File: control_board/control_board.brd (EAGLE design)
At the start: 63 x 73.3 mm, 65 parts, among them IC1 ATMEGA1284P-MU, J1 USB Female Type C Connector, J5 20021311-00010T4LF, J6 20021311-00010T4LF, J7 20021311-00010T4LF, Q2 BSS84-7-F, Q3 BSS138PW,115, SW1 SPST_TACT-KMR2, U1 915MHz, U3 MCP73833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

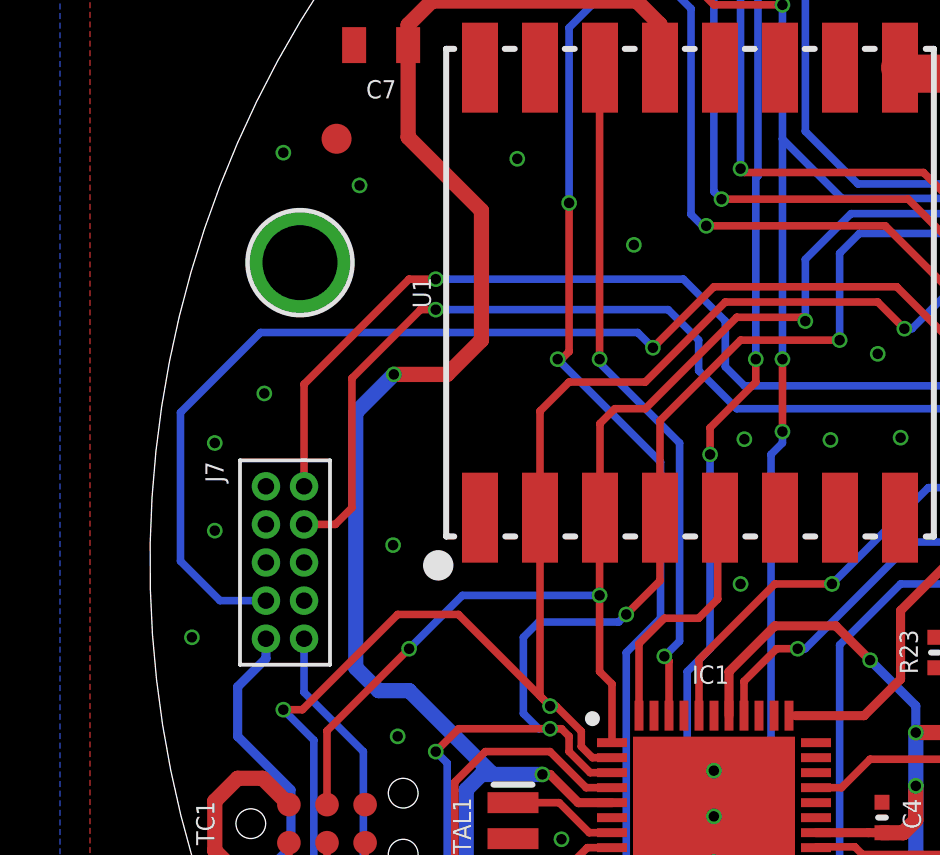
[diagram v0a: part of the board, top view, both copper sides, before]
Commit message: Added pullup on SS pin of radio
- Without pullup, bootloader can't be loaded
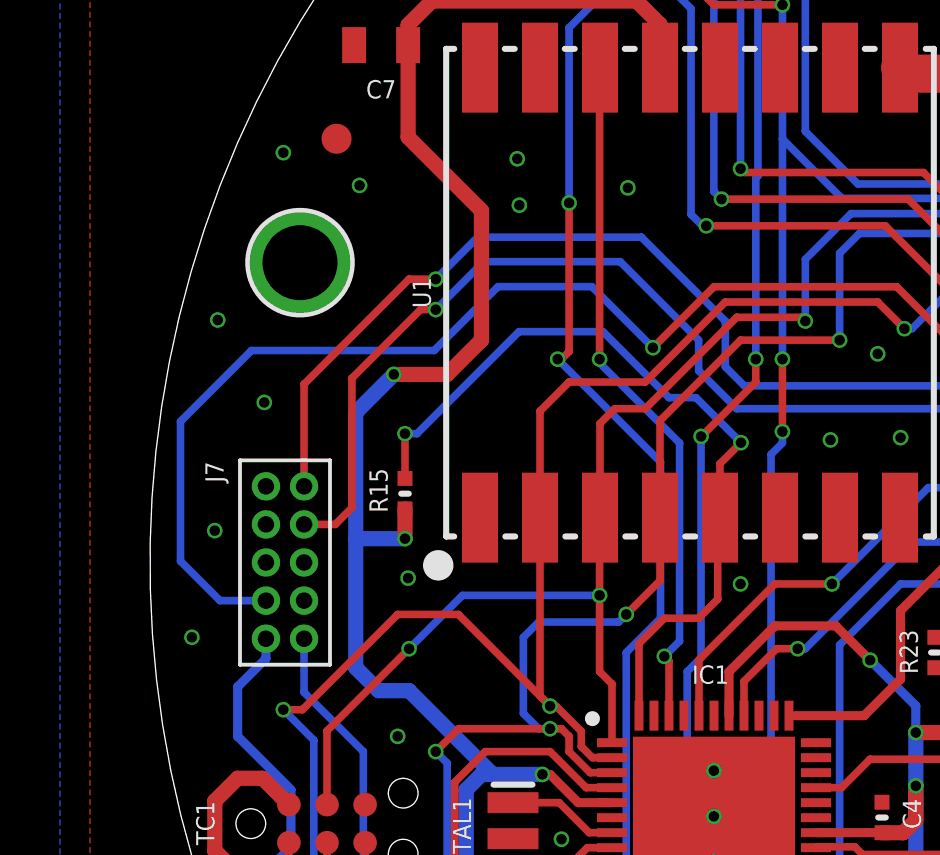
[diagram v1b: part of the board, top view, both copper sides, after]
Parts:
- added R15: 10K, Adafruit Feather 32u4 Bluefruit LE:MICROBUILDER__0402MP
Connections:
- net SS: now also R15.2
- net VCC: now also R15.1
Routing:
- net SS: track 8.39 -> 26.8 mm, vias 0 -> 2
- net VCC: track 175.3 -> 177.9 mm, vias 9 -> 10
- net MOTOR_CONTROL: track 53.8 -> 55.2 mm
- net CURRENT_SENSE_POWER: track 56.5 -> 57.7 mm
- net TEMP: track 56.2 -> 57.3 mm
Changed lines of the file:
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@@
 </layers>
 <board>
-<fusionsync huburn="a.YnVzaW5lc3M6aGF3azI1NA" projecturn="a.YnVzaW5lc3M6aGF3azI1NCMyMDIwMDkxNDMzMjY0NDc4MQ" f3durn="urn:adsk.wipprod:dm.lineage:UtJg9LLlSdqN8RmJzLy1Ng" pcbguid="012a3abc-d9c1-4d21-a72f-0cb22081b20e" lastpulledtime="" lastsyncedchangeguid="" latestrevisionid="7e68664b-9ece-4de8-8436-a87560e4c601" lastsyncedrevisionid="7e68664b-9ece-4de8-8436-a87560e4c601" lastboardhashguid="2f9d8b28-5ca6-9da8-7f9d-c0648b5d30e4" lastpushedtime="2020-11-20T05:35:07Z" linktopcb3d="true"/>
+<fusionsync huburn="a.YnVzaW5lc3M6aGF3azI1NA" projecturn="a.YnVzaW5lc3M6aGF3azI1NCMyMDIwMDkxNDMzMjY0NDc4MQ" f3durn="urn:adsk.wipprod:dm.lineage:UtJg9LLlSdqN8RmJzLy1Ng" pcbguid="" lastpulledtime="" lastsyncedchangeguid="" latestrevisionid="7e68664b-9ece-4de8-8436-a87560e4c601" lastsyncedrevisionid="7e68664b-9ece-4de8-8436-a87560e4c601" lastboardhashguid="2f9d8b28-5ca6-9da8-7f9d-c0648b5d30e4" lastpushedtime="2020-11-20T05:35:07Z" linktopcb3d="true"/>
 <plain>
 <wire x1="35" y1="75" x2="35" y2="-7" width="0.15" layer="49"/>
@@
 <attribute name="PROD_ID" value="CAP-08469" x="7.704" y="52.252" size="1.778" layer="27" display="off"/>
 </element>
+<element name="R15" library="Adafruit Feather 32u4 Bluefruit LE" package="MICROBUILDER__0402MP" override_package3d_urn="urn:adsk.eagle:package:24877243/2" override_package_urn="urn:adsk.eagle:footprint:24877244/1" value="10K" x="8.5" y="37.3" smashed="yes" rot="R90">
+<attribute name="MPN" value="RC0402FR-7W10KL" x="8.5" y="37.3" size="1.778" layer="27" rot="R90" display="off"/>
+<attribute name="NAME" x="7.9237" y="36.665" size="0.6096" layer="25" font="vector" rot="R90"/>
+</element>
 </elements>
 <signals>
@@
 <wire x1="13.081" y1="27.94" x2="11.43" y2="27.94" width="0.508" layer="16"/>
 <wire x1="7.62" y1="30.734" x2="6.858" y2="31.496" width="0.508" layer="16"/>
-<wire x1="6.858" y1="31.496" x2="6.858" y2="40.005" width="0.508" layer="16"/>
+<wire x1="6.858" y1="31.496" x2="6.858" y2="35.8" width="0.508" layer="16"/>
+<wire x1="6.858" y1="35.8" x2="6.858" y2="40.005" width="0.508" layer="16"/>
 <wire x1="6.858" y1="40.005" x2="8.128" y2="41.275" width="0.508" layer="16"/>
 <via x="8.128" y="41.275" extent="1-16" drill="0.35"/>
@@
 <wire x1="8.604" y1="52.252" x2="8.604" y2="52.927" width="0.508" layer="1"/>
 <wire x1="8.604" y1="52.927" x2="9.398" y2="53.721" width="0.508" layer="1"/>
+<contactref element="R15" pad="1"/>
+<wire x1="8.5" y1="36.792" x2="8.5" y2="35.8" width="0.508" layer="1"/>
+<via x="8.5" y="35.8" extent="1-16" drill="0.35"/>
+<wire x1="8.5" y1="35.8" x2="6.858" y2="35.8" width="0.508" layer="16"/>
 </signal>
 <signal name="GND" class="1">
@@
 <via x="26.67" y="30.353" extent="1-16" drill="0.35"/>
 <via x="34.29" y="36.703" extent="1-16" drill="0.35"/>
-<via x="16.129" y="45.593" extent="1-16" drill="0.35"/>
+<via x="15.929" y="47.493" extent="1-16" drill="0.35"/>
 <via x="38.0492" y="13.8684" extent="1-16" drill="0.35"/>
 <via x="38.862" y="13.4366" extent="1-16" drill="0.35"/>
@@
 <via x="6.985" y="47.5742" extent="1-16" drill="0.35"/>
 <via x="46.5074" y="51.0286" extent="1-16" drill="0.35"/>
-<via x="8.1026" y="35.5854" extent="1-16" drill="0.35"/>
+<via x="8.6026" y="34.4854" extent="1-16" drill="0.35"/>
 <via x="13.2842" y="18.5674" extent="1-16" drill="0.35"/>
 <via x="12.4714" y="12.8778" extent="1-16" drill="0.35"/>
@@
 <via x="1.397" y="32.512" extent="1-16" drill="0.35"/>
 <via x="2.159" y="36.068" extent="1-16" drill="0.35"/>
-<via x="2.159" y="38.989" extent="1-16" drill="0.35"/>
-<via x="3.81" y="40.64" extent="1-16" drill="0.35"/>
+<via x="2.259" y="43.089" extent="1-16" drill="0.35"/>
+<via x="3.81" y="40.34" extent="1-16" drill="0.35"/>
 <via x="26.67" y="49.965" extent="1-16" drill="0.35"/>
 <via x="27.94" y="49.965" extent="1-16" drill="0.35"/>
@@
 <wire x1="22.86" y1="54.7767125" x2="22.2647125" y2="55.372" width="0.254" layer="1"/>
 <via x="19.685" y="34.29" extent="1-16" drill="0.35"/>
-<via x="19.812" y="39.116" extent="1-16" drill="0.35"/>
+<via x="12.312" y="46.916" extent="1-16" drill="0.35"/>
 <wire x1="19.3" y1="23.1" x2="19.3" y2="24.515" width="0.254" layer="1"/>
 <wire x1="19.3" y1="24.515" x2="18.796" y2="25.019" width="0.254" layer="1"/>
@@
 <via x="20.193" y="41.783" extent="1-16" drill="0.35"/>
 <wire x1="20.193" y1="41.783" x2="20.193" y2="41.021" width="0.254" layer="1"/>
-<wire x1="20.193" y1="41.021" x2="18.669" y2="39.497" width="0.254" layer="1"/>
-<wire x1="18.669" y1="39.497" x2="18.669" y2="38.608" width="0.254" layer="1"/>
-<via x="18.669" y="38.608" extent="1-16" drill="0.35"/>
-<wire x1="18.669" y1="32.131" x2="18.669" y2="38.608" width="0.254" layer="16"/>
+<wire x1="20.193" y1="41.021" x2="18.38" y2="39.208" width="0.254" layer="1"/>
+<wire x1="18.38" y1="39.208" x2="18.369" y2="39.208" width="0.254" layer="1"/>
+<via x="18.369" y="39.208" extent="1-16" drill="0.35"/>
+<wire x1="18.369" y1="31.831" x2="18.369" y2="39.208" width="0.254" layer="16"/>
 <wire x1="19.558" y1="21.59" x2="17.907" y2="23.241" width="0.254" layer="16"/>
-<wire x1="17.907" y1="31.369" x2="18.669" y2="32.131" width="0.254" layer="16"/>
+<wire x1="17.907" y1="31.369" x2="18.369" y2="31.831" width="0.254" layer="16"/>
 <wire x1="17.907" y1="23.241" x2="17.907" y2="31.369" width="0.254" layer="16"/>
 <wire x1="42.955" y1="54.135" x2="42.5018" y2="54.135" width="0.254" layer="16"/>
@@
 <wire x1="16.3" y1="32.302" x2="17.145" y2="33.147" width="0.254" layer="1"/>
 <wire x1="18.923" y1="33.782" x2="18.923" y2="36.423" width="0.254" layer="1"/>
+<contactref element="R15" pad="2"/>
+<wire x1="19" y1="36.5" x2="19" y2="38.3" width="0.254" layer="1"/>
+<wire x1="19" y1="38.3" x2="19.7" y2="39" width="0.254" layer="1"/>
+<via x="19.7" y="39" extent="1-16" drill="0.35"/>
+<wire x1="19.7" y1="39" x2="18.2" y2="40.5" width="0.254" layer="16"/>
+<wire x1="8.9" y1="39.3" x2="8.5" y2="39.3" width="0.254" layer="16"/>
+<via x="8.5" y="39.3" extent="1-16" drill="0.35"/>
+<wire x1="8.5" y1="39.3" x2="8.5" y2="37.808" width="0.254" layer="1"/>
+<wire x1="18.2" y1="40.5" x2="17.3" y2="40.5" width="0.254" layer="16"/>
+<wire x1="17.3" y1="40.5" x2="15.1" y2="42.7" width="0.254" layer="16"/>
+<wire x1="15.1" y1="42.7" x2="12.3" y2="42.7" width="0.254" layer="16"/>
+<wire x1="12.3" y1="42.7" x2="8.9" y2="39.3" width="0.254" layer="16"/>
 </signal>
 <signal name="MOSI">
@@
 <wire x1="18.796" y1="44.196" x2="16.764" y2="42.164" width="0.254" layer="1"/>
 <via x="16.764" y="42.164" extent="1-16" drill="0.35"/>
-<wire x1="16.764" y1="42.164" x2="16.256" y2="42.672" width="0.254" layer="16"/>
-<wire x1="16.256" y1="42.672" x2="3.683" y2="42.672" width="0.254" layer="16"/>
-<wire x1="1.016" y1="40.005" x2="1.016" y2="35.052" width="0.254" layer="16"/>
+<wire x1="1.016" y1="39.705" x2="1.016" y2="35.052" width="0.254" layer="16"/>
 <wire x1="1.016" y1="35.052" x2="2.333" y2="33.735" width="0.254" layer="16"/>
 <wire x1="29.464" y1="36.449" x2="29.464" y2="39.624" width="0.254" layer="1"/>
 <wire x1="29.464" y1="39.624" x2="24.892" y2="44.196" width="0.254" layer="1"/>
-<wire x1="3.683" y1="42.672" x2="1.016" y2="40.005" width="0.254" layer="16"/>
+<wire x1="3.383" y1="42.072" x2="1.016" y2="39.705" width="0.254" layer="16"/>
 <wire x1="2.333" y1="33.735" x2="3.865" y2="33.735" width="0.254" layer="16"/>
 <wire x1="21.3" y1="29.9" x2="21.518" y2="29.9" width="0.254" layer="1"/>
@@
 <wire x1="23.804" y1="29.9" x2="25.019" y2="31.115" width="0.3048" layer="1"/>
 <wire x1="25.019" y1="31.115" x2="25.019" y2="33.401" width="0.3048" layer="1"/>
+<wire x1="9.472" y1="42.072" x2="3.383" y2="42.072" width="0.254" layer="16"/>
+<wire x1="16.764" y1="42.164" x2="14.728" y2="44.2" width="0.254" layer="16"/>
+<wire x1="14.728" y1="44.2" x2="11.6" y2="44.2" width="0.254" layer="16"/>
+<wire x1="11.6" y1="44.2" x2="9.472" y2="42.072" width="0.254" layer="16"/>
 </signal>
 <signal name="A">
@@
 <wire x1="31.115" y1="33.147" x2="26.543" y2="28.575" width="0.254" layer="16"/>
 <wire x1="26.543" y1="24.638" x2="23.749" y2="24.638" width="0.254" layer="1"/>
-<wire x1="9.525" y1="43.434" x2="17.272" y2="43.434" width="0.254" layer="16"/>
+<wire x1="15.672" y1="45.034" x2="11.125" y2="45.034" width="0.254" layer="16"/>
+<wire x1="9.525" y1="43.434" x2="11.125" y2="45.034" width="0.254" layer="16"/>
 <wire x1="18.288" y1="42.418" x2="18.288" y2="41.402" width="0.254" layer="16"/>
 <wire x1="19.558" y1="40.132" x2="18.288" y2="41.402" width="0.254" layer="16"/>
 <wire x1="28.575" y1="40.132" x2="31.115" y2="37.592" width="0.254" layer="16"/>
-<wire x1="17.272" y1="43.434" x2="18.288" y2="42.418" width="0.254" layer="16"/>
+<wire x1="15.672" y1="45.034" x2="18.288" y2="42.418" width="0.254" layer="16"/>
 <wire x1="19.558" y1="40.132" x2="28.575" y2="40.132" width="0.254" layer="16"/>
 </signal>
@@
 <wire x1="26.924" y1="23.749" x2="27.178" y2="24.003" width="0.254" layer="1"/>
 <wire x1="23.622" y1="24.13" x2="25.654" y2="24.13" width="0.254" layer="1"/>
-<wire x1="9.525" y1="44.45" x2="17.78" y2="44.45" width="0.254" layer="16"/>
+<wire x1="16.38" y1="45.85" x2="10.925" y2="45.85" width="0.254" layer="16"/>
+<wire x1="9.525" y1="44.45" x2="10.925" y2="45.85" width="0.254" layer="16"/>
 <wire x1="19.177" y1="43.053" x2="19.177" y2="41.529" width="0.254" layer="16"/>
 <wire x1="19.177" y1="41.529" x2="19.812" y2="40.894" width="0.254" layer="16"/>
-<wire x1="17.78" y1="44.45" x2="19.177" y2="43.053" width="0.254" layer="16"/>
+<wire x1="16.38" y1="45.85" x2="19.177" y2="43.053" width="0.254" layer="16"/>
 <wire x1="28.956" y1="40.894" x2="31.877" y2="37.973" width="0.254" layer="16"/>
 <wire x1="31.877" y1="37.973" x2="31.877" y2="32.766" width="0.254" layer="16"/>

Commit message: v0.3 - fixed VIN power
- Changed VBAT to VIN on headers so the power board works even when there is no battery present
- Changed resistor dividor traces so it connects to proper VBAT circuit
- small trace and silkscreen modifications
- updated gerbers
- ERC/DRC
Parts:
- moved R18 0.38 mm to (45.5, 13.3), turned to 270 degrees
- moved R17 0.21 mm to (43.7, 13.3), turned to 270 degrees
- moved C9 0.20 mm to (47.5, 13.3), turned to 270 degrees
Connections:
- net VBAT: no longer J5.10, J5.7, J5.8, J5.9
- net VIN: now also J5.10, J5.7, J5.8, J5.9
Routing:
- net VIN: track 17.4 -> 48.9 mm, vias 2 -> 3
- net VBAT: track 53.8 -> 43.7 mm
- net VBUS: track 95.6 -> 89.8 mm, vias 5 -> 4
- net N$8: track 15.7 -> 17.8 mm
- net N$13: track 15.2 -> 13.9 mm
- net VBAT_SENSE: track 45.1 -> 44.4 mm
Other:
- board text added: "v0.3 2020-11-24"
- board text removed: "v0.1 2020-11-16"

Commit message: v0.4 - added pullup on flash SS
- flash SS now has pullup to allow bootload while flash is installed
- updated gerbers only
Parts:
- added R24: 10K, Adafruit Feather 32u4 Bluefruit LE:MICROBUILDER__0402MP
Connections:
- net CS: now also R24.2
- net VCC: now also R24.1
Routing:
- net VCC: track 177.9 -> 181.5 mm
- net CS: track 33.7 -> 35.5 mm
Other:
- board text added: "v0.4 2020-11-26"
- board text removed: "v0.3 2020-11-24"
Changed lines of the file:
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@@
 </layers>
 <board>
-<fusionsync huburn="a.YnVzaW5lc3M6aGF3azI1NA" projecturn="a.YnVzaW5lc3M6aGF3azI1NCMyMDIwMDkxNDMzMjY0NDc4MQ" f3durn="urn:adsk.wipprod:dm.lineage:UtJg9LLlSdqN8RmJzLy1Ng" pcbguid="" lastpulledtime="" lastsyncedchangeguid="" latestrevisionid="7e68664b-9ece-4de8-8436-a87560e4c601" lastsyncedrevisionid="7e68664b-9ece-4de8-8436-a87560e4c601" lastboardhashguid="2f9d8b28-5ca6-9da8-7f9d-c0648b5d30e4" lastpushedtime="2020-11-20T05:35:07Z" linktopcb3d="true"/>
+<fusionsync huburn="a.YnVzaW5lc3M6aGF3azI1NA" projecturn="a.YnVzaW5lc3M6aGF3azI1NCMyMDIwMDkxNDMzMjY0NDc4MQ" f3durn="urn:adsk.wipprod:dm.lineage:UtJg9LLlSdqN8RmJzLy1Ng" pcbguid="" lastpulledtime="" lastsyncedchangeguid="" latestrevisionid="7e68664b-9ece-4de8-8436-a87560e4c601" lastsyncedrevisionid="7e68664b-9ece-4de8-8436-a87560e4c601" lastboardhashguid="2f9d8b28-5ca6-9da8-7f9d-c0648b5d30e4" lastpushedtime="2020-11-20T05:35:07Z" linktopcb3d="false"/>
 <plain>
 <wire x1="35" y1="75" x2="35" y2="-7" width="0.15" layer="49"/>
@@
 <text x="44.339209375" y="65.2526" size="1.27" layer="21" font="vector" ratio="20" align="bottom-center">BORC</text>
 <text x="44.339209375" y="63.9572" size="0.8128" layer="21" font="vector" align="bottom-center">Control Board</text>
-<text x="44.313809375" y="61.468" size="0.6096" layer="21" font="vector" align="bottom-center">v0.3
-2020-11-24</text>
+<text x="44.313809375" y="61.468" size="0.6096" layer="21" font="vector" align="bottom-center">v0.4
+2020-11-26</text>
 <text x="18.075609375" y="58.6486" size="0.6096" layer="21" font="vector">&lt;- LED screen conn.
     (contacts face down)</text>
@@
 <attribute name="NAME" x="7.9237" y="36.665" size="0.6096" layer="25" font="vector" rot="R90"/>
 </element>
+<element name="R24" library="Adafruit Feather 32u4 Bluefruit LE" package="MICROBUILDER__0402MP" override_package3d_urn="urn:adsk.eagle:package:24877243/2" override_package_urn="urn:adsk.eagle:footprint:24877244/1" value="10K" x="46.101" y="41.529" smashed="yes">
+<attribute name="MPN" value="RC0402FR-7W10KL" x="46.101" y="41.529" size="1.778" layer="27" display="off"/>
+<attribute name="NAME" x="45.466" y="42.1323" size="0.6096" layer="25" font="vector"/>
+</element>
 </elements>
 <signals>
@@
 <via x="8.5" y="35.8" extent="1-16" drill="0.35"/>
 <wire x1="8.5" y1="35.8" x2="6.858" y2="35.8" width="0.508" layer="16"/>
+<contactref element="R24" pad="1"/>
+<wire x1="45.593" y1="41.529" x2="42.545" y2="41.529" width="0.508" layer="1"/>
+<wire x1="42.545" y1="41.529" x2="42.1941125" y2="41.8798875" width="0.508" layer="1"/>
 </signal>
 <signal name="GND" class="1">
@@
 <via x="45.847" y="28.956" extent="1-16" drill="0.35"/>
 <via x="38.481" y="34.798" extent="1-16" drill="0.35"/>
-<via x="47.625" y="40.767" extent="1-16" drill="0.35"/>
+<via x="48.387" y="40.64" extent="1-16" drill="0.35"/>
 <via x="46.6344" y="49.5046" extent="1-16" drill="0.35"/>
 <via x="32.9692" y="20.4724" extent="1-16" drill="0.35"/>
@@
 <wire x1="22.227" y1="25.527" x2="23.495" y2="25.527" width="0.254" layer="1"/>
 <wire x1="23.749" y1="25.273" x2="23.495" y2="25.527" width="0.254" layer="1"/>
-<wire x1="46.6162" y1="44.095" x2="46.6162" y2="43.3142" width="0.254" layer="1"/>
-<wire x1="46.6162" y1="43.3142" x2="43.434" y2="40.132" width="0.254" layer="1"/>
-<wire x1="43.434" y1="40.132" x2="41.275" y2="40.132" width="0.254" layer="1"/>
-<wire x1="41.275" y1="40.132" x2="29.591" y2="28.448" width="0.254" layer="1"/>
+<wire x1="46.6162" y1="43.6952" x2="46.6162" y2="44.095" width="0.254" layer="1"/>
+<wire x1="40.767" y1="39.624" x2="29.591" y2="28.448" width="0.254" layer="1"/>
 <wire x1="29.591" y1="28.448" x2="29.591" y2="26.924" width="0.254" layer="1"/>
 <wire x1="29.591" y1="26.924" x2="27.94" y2="25.273" width="0.254" layer="1"/>
 <wire x1="27.94" y1="25.273" x2="23.749" y2="25.273" width="0.254" layer="1"/>
+<contactref element="R24" pad="2"/>
+<wire x1="46.609" y1="41.529" x2="46.609" y2="43.688" width="0.254" layer="1"/>
+<wire x1="46.609" y1="43.688" x2="46.6162" y2="43.6952" width="0.254" layer="1"/>
+<wire x1="46.609" y1="41.529" x2="46.609" y2="40.259" width="0.254" layer="1"/>
+<wire x1="45.974" y1="39.624" x2="40.767" y2="39.624" width="0.254" layer="1"/>
+<wire x1="46.609" y1="40.259" x2="45.974" y2="39.624" width="0.254" layer="1"/>
 </signal>
 <signal name="VBAT_SENSE">
